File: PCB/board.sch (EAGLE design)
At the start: 9 parts, among them J1 PROG-HEADER_2X3_SHROUDED, J10 PROG-HEADER_2X5_1.27MM-SHROUD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, J2 PROG-HEADER_2X5_2.00MM-SHROUD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, J3 PROG-HEADER_2X5_SHROUDED, J5 PROG-HEADER_2X10_RIGHT-ANGLE, J6 PROG-HEADER_2X10_SHROUDED, J8 CONN-1X4, J9 CONN-1X6

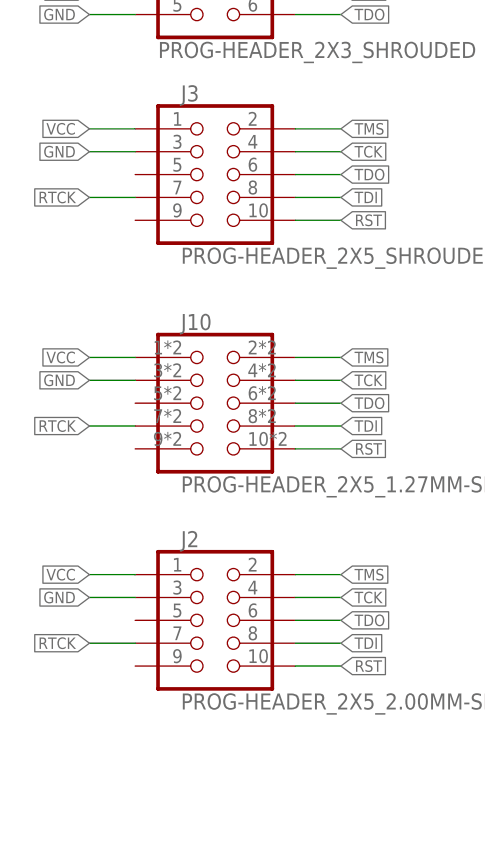
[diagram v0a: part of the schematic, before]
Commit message: connected pin 5, 9 to GND
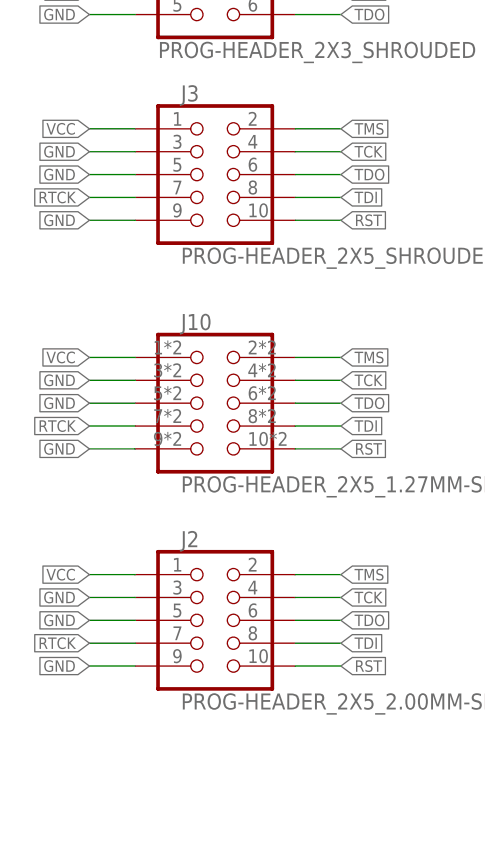
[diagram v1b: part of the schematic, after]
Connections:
- net GND: now also J10.5, J10.9, J2.5, J2.9, J3.5, J3.9
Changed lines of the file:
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@@
 <wire x1="207.01" y1="116.84" x2="201.93" y2="116.84" width="0.1524" layer="91"/>
+</segment>
+<segment>
+<wire x1="54.61" y1="123.19" x2="49.53" y2="123.19" width="0.1524" layer="91"/>
+<label x="49.53" y="123.19" size="1.27" layer="95" rot="R180" xref="yes"/>
+<pinref part="J3" gate="G$1" pin="5"/>
+</segment>
+<segment>
+<wire x1="54.61" y1="118.11" x2="49.53" y2="118.11" width="0.1524" layer="91"/>
+<label x="49.53" y="118.11" size="1.27" layer="95" rot="R180" xref="yes"/>
+<pinref part="J3" gate="G$1" pin="9"/>
+</segment>
+<segment>
+<wire x1="54.61" y1="97.79" x2="49.53" y2="97.79" width="0.1524" layer="91"/>
+<label x="49.53" y="97.79" size="1.27" layer="95" rot="R180" xref="yes"/>
+<pinref part="J10" gate="G$1" pin="5"/>
+</segment>
+<segment>
+<wire x1="54.61" y1="92.71" x2="49.53" y2="92.71" width="0.1524" layer="91"/>
+<label x="49.53" y="92.71" size="1.27" layer="95" rot="R180" xref="yes"/>
+<pinref part="J10" gate="G$1" pin="9"/>
+</segment>
+<segment>
+<wire x1="54.61" y1="73.66" x2="49.53" y2="73.66" width="0.1524" layer="91"/>
+<label x="49.53" y="73.66" size="1.27" layer="95" rot="R180" xref="yes"/>
+<pinref part="J2" gate="G$1" pin="5"/>
+</segment>
+<segment>
+<wire x1="54.61" y1="68.58" x2="49.53" y2="68.58" width="0.1524" layer="91"/>
+<label x="49.53" y="68.58" size="1.27" layer="95" rot="R180" xref="yes"/>
+<pinref part="J2" gate="G$1" pin="9"/>
 </segment>
 </net>

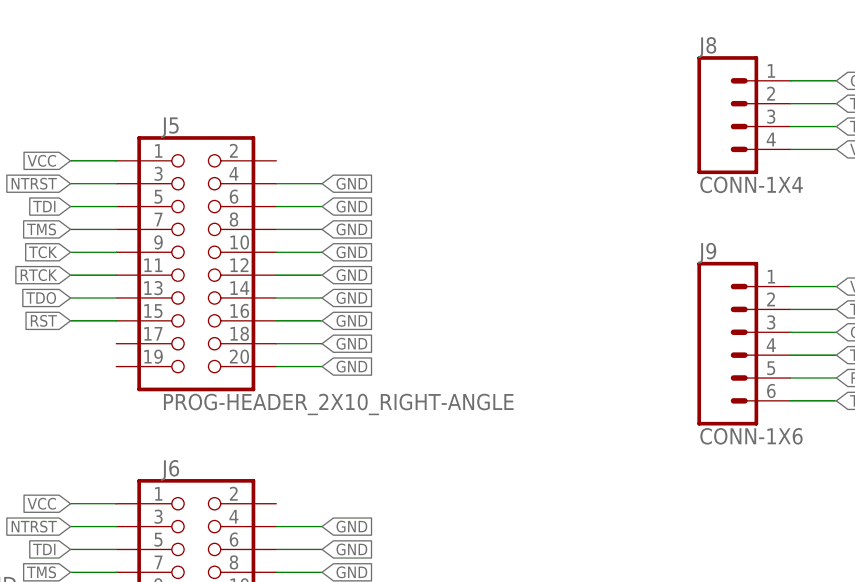
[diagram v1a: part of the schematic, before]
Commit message: changed right angle connector to end launch
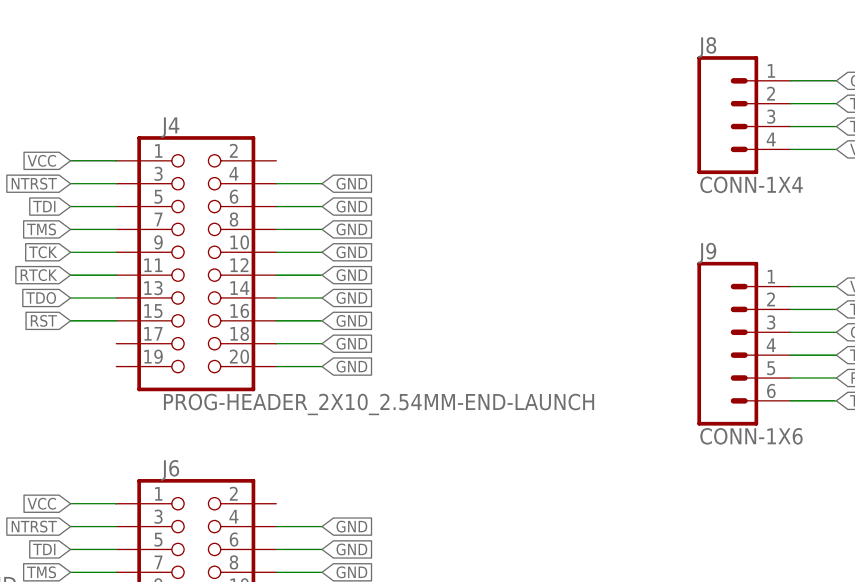
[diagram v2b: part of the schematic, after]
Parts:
- removed J5: PROG-HEADER_2X10_RIGHT-ANGLE, angrypig7-Connectors-Programming:PROG-HEADER_2X10_RIGHT-ANGLE
- added J4: PROG-HEADER_2X10_2.54MM-END-LAUNCH, angrypig7-Connectors-Programming:PROG-HEADER_2X10_2.54MM-END-LAUNCH
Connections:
- net GND: now also J4.10, J4.12, J4.14, J4.16, J4.18, J4.20, J4.4, J4.6, J4.8; no longer J5.10, J5.12, J5.14, J5.16, J5.18, J5.20, J5.4, J5.6, J5.8
- net NTRST: now also J4.3; no longer J5.3
- net RST: now also J4.15; no longer J5.15
- net RTCK: now also J4.11; no longer J5.11
- net TCK: now also J4.9; no longer J5.9
- net TDI: now also J4.5; no longer J5.5
- net TDO: now also J4.13; no longer J5.13
- net TMS: now also J4.7; no longer J5.7
- net VCC: now also J4.1; no longer J5.1
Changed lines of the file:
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@@
 <?xml version="1.0" encoding="utf-8"?>
 <!DOCTYPE eagle SYSTEM "eagle.dtd">
-<eagle version="9.6.0">
+<eagle version="9.6.1">
 <drawing>
 <settings>
@@
 <setting verticaltext="up"/>
 </settings>
-<grid distance="0.1" unitdist="inch" unit="inch" style="lines" multiple="1" display="no" altdistance="0.01" altunitdist="inch" altunit="inch"/>
+<grid distance="50" unitdist="mil" unit="mil" style="lines" multiple="1" display="no" altdistance="0.01" altunitdist="inch" altunit="inch"/>
 <layers>
 <layer number="1" name="Top" color="4" fill="1" visible="no" active="no"/>
@@
 <part name="J10" library="angrypig7-Connectors-Programming" deviceset="PROG-HEADER_2X5" device="_1.27MM-SHROUDED_PTH_SMD" value="PROG-HEADER_2X5_1.27MM-SHROUDED_PTH_SMD"/>
 <part name="J2" library="angrypig7-Connectors-Programming" deviceset="PROG-HEADER_2X5" device="_2.00MM-SHROUDED"/>
-<part name="J5" library="angrypig7-Connectors-Programming" deviceset="PROG-HEADER_2X10" device="_RIGHT-ANGLE"/>
+<part name="J4" library="angrypig7-Connectors-Programming" deviceset="PROG-HEADER_2X10" device="_2.54MM-END-LAUNCH"/>
 </parts>
 <sheets>
@@
 <attribute name="VALUE" x="59.69" y="63.754" size="1.778" layer="96" font="vector"/>
 </instance>
-<instance part="J5" gate="G$1" x="135.89" y="124.46" smashed="yes">
+<instance part="J4" gate="G$1" x="135.89" y="124.46" smashed="yes">
 <attribute name="NAME" x="132.08" y="138.938" size="1.778" layer="95" font="vector"/>
 <attribute name="VALUE" x="132.08" y="108.204" size="1.778" layer="96" font="vector"/>
@@
 <wire x1="127" y1="135.89" x2="121.92" y2="135.89" width="0.1524" layer="91"/>
 <label x="121.92" y="135.89" size="1.27" layer="95" rot="R180" xref="yes"/>
-<pinref part="J5" gate="G$1" pin="1"/>
+<pinref part="J4" gate="G$1" pin="1"/>
 </segment>
 </net>
@@
 <wire x1="127" y1="128.27" x2="121.92" y2="128.27" width="0.1524" layer="91"/>
 <label x="121.92" y="128.27" size="1.27" layer="95" rot="R180" xref="yes"/>
-<pinref part="J5" gate="G$1" pin="7"/>
+<pinref part="J4" gate="G$1" pin="7"/>
 </segment>
 <segment>
@@
 <wire x1="127" y1="120.65" x2="121.92" y2="120.65" width="0.1524" layer="91"/>
 <label x="121.92" y="120.65" size="1.27" layer="95" rot="R180" xref="yes"/>
-<pinref part="J5" gate="G$1" pin="13"/>
+<pinref part="J4" gate="G$1" pin="13"/>
 </segment>
 <segment>
@@
 <wire x1="127" y1="130.81" x2="121.92" y2="130.81" width="0.1524" layer="91"/>
 <label x="121.92" y="130.81" size="1.27" layer="95" rot="R180" xref="yes"/>
-<pinref part="J5" gate="G$1" pin="5"/>
+<pinref part="J4" gate="G$1" pin="5"/>
 </segment>
 </net>
@@
 <wire x1="127" y1="118.11" x2="121.92" y2="118.11" width="0.1524" layer="91"/>
 <label x="121.92" y="118.11" size="1.27" layer="95" rot="R180" xref="yes"/>
-<pinref part="J5" gate="G$1" pin="15"/>
+<pinref part="J4" gate="G$1" pin="15"/>
 </segment>
 <segment>
@@
 <wire x1="144.78" y1="133.35" x2="149.86" y2="133.35" width="0.1524" layer="91"/>
 <label x="149.86" y="133.35" size="1.27" layer="95" xref="yes"/>
-<pinref part="J5" gate="G$1" pin="4"/>
+<pinref part="J4" gate="G$1" pin="4"/>
 </segment>
 <segment>
 <wire x1="144.78" y1="130.81" x2="149.86" y2="130.81" width="0.1524" layer="91"/>
 <label x="149.86" y="130.81" size="1.27" layer="95" xref="yes"/>
-<pinref part="J5" gate="G$1" pin="6"/>
+<pinref part="J4" gate="G$1" pin="6"/>
 </segment>
 <segment>
 <wire x1="144.78" y1="113.03" x2="149.86" y2="113.03" width="0.1524" layer="91"/>
 <label x="149.86" y="113.03" size="1.27" layer="95" xref="yes"/>
-<pinref part="J5" gate="G$1" pin="20"/>
+<pinref part="J4" gate="G$1" pin="20"/>
 </segment>
 <segment>
 <wire x1="144.78" y1="115.57" x2="149.86" y2="115.57" width="0.1524" layer="91"/>
 <label x="149.86" y="115.57" size="1.27" layer="95" xref="yes"/>
-<pinref part="J5" gate="G$1" pin="18"/>
+<pinref part="J4" gate="G$1" pin="18"/>
 </segment>
 <segment>
 <wire x1="144.78" y1="118.11" x2="149.86" y2="118.11" width="0.1524" layer="91"/>
 <label x="149.86" y="118.11" size="1.27" layer="95" xref="yes"/>
-<pinref part="J5" gate="G$1" pin="16"/>
+<pinref part="J4" gate="G$1" pin="16"/>
 </segment>
 <segment>
 <wire x1="144.78" y1="120.65" x2="149.86" y2="120.65" width="0.1524" layer="91"/>
 <label x="149.86" y="120.65" size="1.27" layer="95" xref="yes"/>
-<pinref part="J5" gate="G$1" pin="14"/>
+<pinref part="J4" gate="G$1" pin="14"/>
 </segment>
 <segment>
 <wire x1="144.78" y1="123.19" x2="149.86" y2="123.19" width="0.1524" layer="91"/>
 <label x="149.86" y="123.19" size="1.27" layer="95" xref="yes"/>
-<pinref part="J5" gate="G$1" pin="12"/>
+<pinref part="J4" gate="G$1" pin="12"/>
 </segment>
 <segment>
 <wire x1="144.78" y1="125.73" x2="149.86" y2="125.73" width="0.1524" layer="91"/>
 <label x="149.86" y="125.73" size="1.27" layer="95" xref="yes"/>
-<pinref part="J5" gate="G$1" pin="10"/>
+<pinref part="J4" gate="G$1" pin="10"/>
 </segment>
 <segment>
 <wire x1="144.78" y1="128.27" x2="149.86" y2="128.27" width="0.1524" layer="91"/>
 <label x="149.86" y="128.27" size="1.27" layer="95" xref="yes"/>
-<pinref part="J5" gate="G$1" pin="8"/>
+<pinref part="J4" gate="G$1" pin="8"/>
 </segment>
 <segment>
@@
 <wire x1="127" y1="123.19" x2="121.92" y2="123.19" width="0.1524" layer="91"/>
 <label x="121.92" y="123.19" size="1.27" layer="95" rot="R180" xref="yes"/>
-<pinref part="J5" gate="G$1" pin="11"/>
+<pinref part="J4" gate="G$1" pin="11"/>
 </segment>
 </net>
@@
 <wire x1="127" y1="125.73" x2="121.92" y2="125.73" width="0.1524" layer="91"/>
 <label x="121.92" y="125.73" size="1.27" layer="95" rot="R180" xref="yes"/>
-<pinref part="J5" gate="G$1" pin="9"/>
+<pinref part="J4" gate="G$1" pin="9"/>
 </segment>
 <segment>
@@
 <net name="NTRST" class="0">
 <segment>
-<pinref part="J5" gate="G$1" pin="3"/>
 <wire x1="127" y1="133.35" x2="121.92" y2="133.35" width="0.1524" layer="91"/>
 <label x="121.92" y="133.35" size="1.27" layer="95" rot="R180" xref="yes"/>
-</segment>
-<segment>
+<pinref part="J4" gate="G$1" pin="3"/>
+</segment>
+<segment>

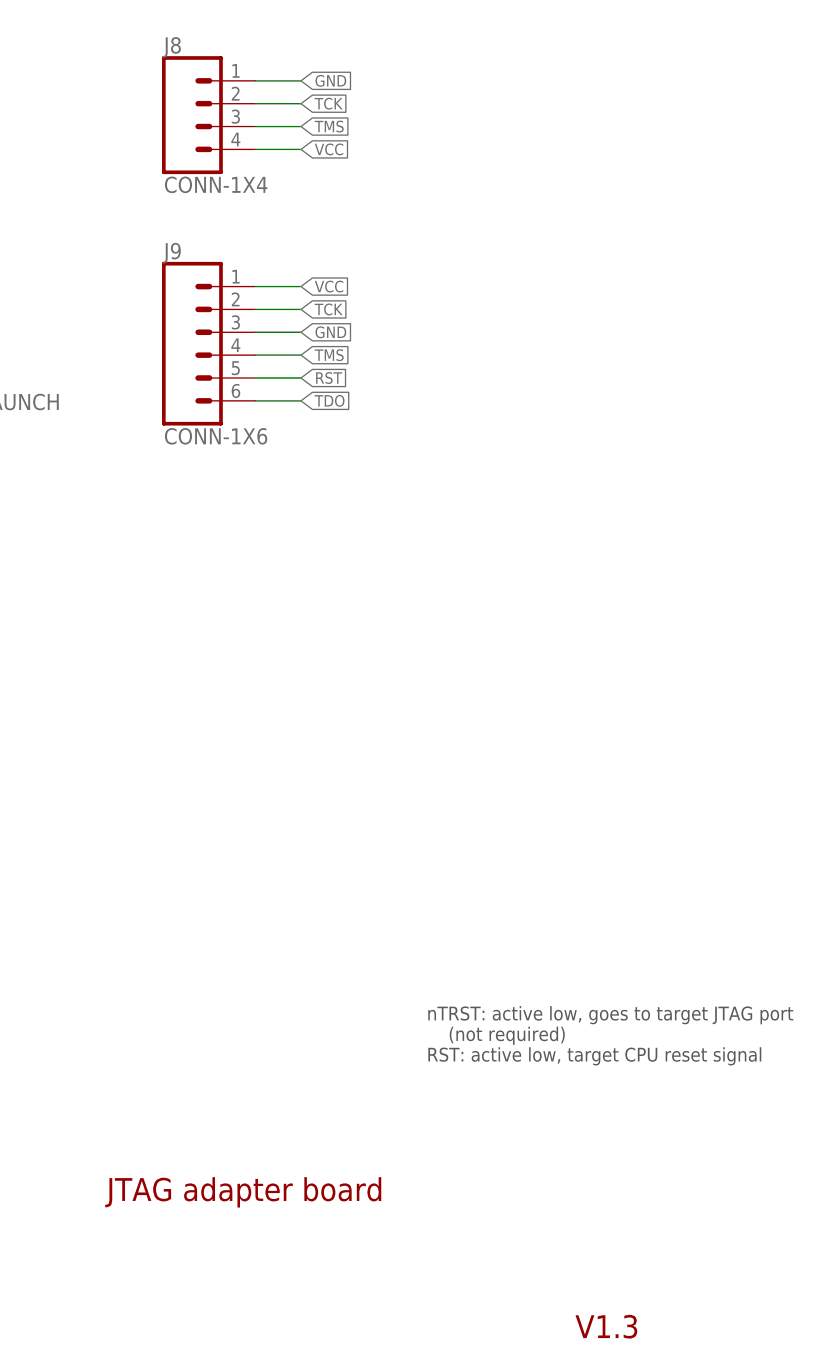
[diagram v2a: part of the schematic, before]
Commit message: fixed footprint error
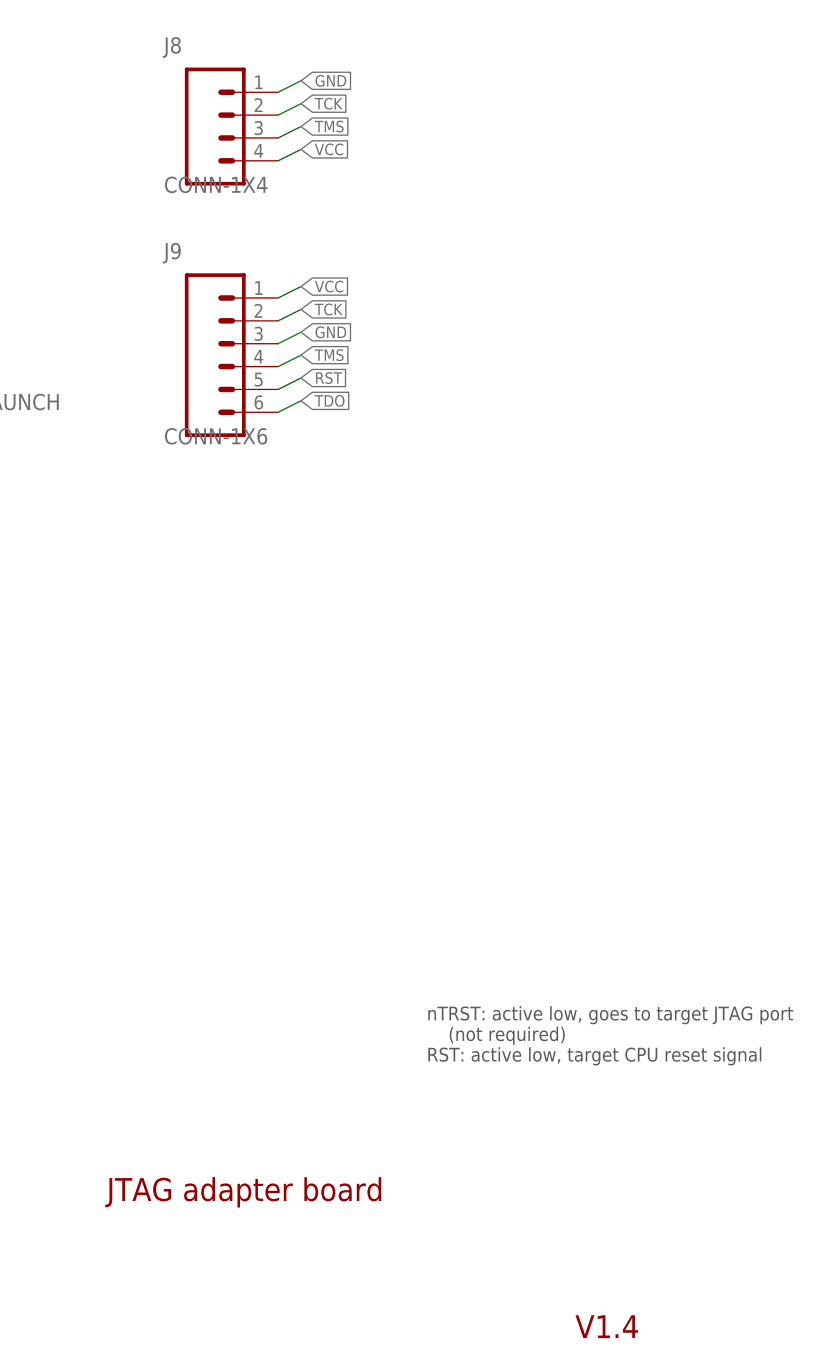
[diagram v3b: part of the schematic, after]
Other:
- moved on the sheet: J8, J9
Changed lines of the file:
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@@
 <attributes>
 <attribute name="CNAME" value="JTAG adapter board"/>
-<attribute name="CREVISION" value="V1.3"/>
+<attribute name="CREVISION" value="V1.4"/>
 </attributes>
 <variantdefs>
@@
 </segment>
 <segment>
-<wire x1="201.93" y1="137.16" x2="207.01" y2="137.16" width="0.1524" layer="91"/>
+<wire x1="204.47" y1="135.89" x2="207.01" y2="137.16" width="0.1524" layer="91"/>
 <label x="207.01" y="137.16" size="1.27" layer="95" xref="yes"/>
 <pinref part="J8" gate="G$1" pin="4"/>
@@
 <label x="207.01" y="121.92" size="1.27" layer="95" xref="yes"/>
 <pinref part="J9" gate="G$1" pin="1"/>
-<wire x1="207.01" y1="121.92" x2="201.93" y2="121.92" width="0.1524" layer="91"/>
+<wire x1="207.01" y1="121.92" x2="204.47" y2="120.65" width="0.1524" layer="91"/>
 </segment>
 <segment>
@@
 </segment>
 <segment>
-<wire x1="201.93" y1="139.7" x2="207.01" y2="139.7" width="0.1524" layer="91"/>
+<wire x1="204.47" y1="138.43" x2="207.01" y2="139.7" width="0.1524" layer="91"/>
 <label x="207.01" y="139.7" size="1.27" layer="95" xref="yes"/>
 <pinref part="J8" gate="G$1" pin="3"/>
@@
 <label x="207.01" y="114.3" size="1.27" layer="95" xref="yes"/>
 <pinref part="J9" gate="G$1" pin="4"/>
-<wire x1="201.93" y1="114.3" x2="207.01" y2="114.3" width="0.1524" layer="91"/>
+<wire x1="204.47" y1="113.03" x2="207.01" y2="114.3" width="0.1524" layer="91"/>
 </segment>
 </net>
@@
 <label x="207.01" y="109.22" size="1.27" layer="95" xref="yes"/>
 <pinref part="J9" gate="G$1" pin="6"/>
-<wire x1="201.93" y1="109.22" x2="207.01" y2="109.22" width="0.1524" layer="91"/>
+<wire x1="204.47" y1="107.95" x2="207.01" y2="109.22" width="0.1524" layer="91"/>
 </segment>
 </net>
@@
 <label x="207.01" y="111.76" size="1.27" layer="95" xref="yes"/>
 <pinref part="J9" gate="G$1" pin="5"/>
-<wire x1="201.93" y1="111.76" x2="207.01" y2="111.76" width="0.1524" layer="91"/>
+<wire x1="204.47" y1="110.49" x2="207.01" y2="111.76" width="0.1524" layer="91"/>
 </segment>
 </net>
@@
 </segment>
 <segment>
-<wire x1="201.93" y1="144.78" x2="207.01" y2="144.78" width="0.1524" layer="91"/>
+<wire x1="204.47" y1="143.51" x2="207.01" y2="144.78" width="0.1524" layer="91"/>
 <label x="207.01" y="144.78" size="1.27" layer="95" xref="yes"/>
 <pinref part="J8" gate="G$1" pin="1"/>
@@
 <label x="207.01" y="116.84" size="1.27" layer="95" xref="yes"/>
 <pinref part="J9" gate="G$1" pin="3"/>
-<wire x1="207.01" y1="116.84" x2="201.93" y2="116.84" width="0.1524" layer="91"/>
+<wire x1="207.01" y1="116.84" x2="204.47" y2="115.57" width="0.1524" layer="91"/>
 </segment>
 <segment>
@@
 <net name="TCK" class="0">
 <segment>
-<wire x1="201.93" y1="142.24" x2="207.01" y2="142.24" width="0.1524" layer="91"/>
+<wire x1="204.47" y1="140.97" x2="207.01" y2="142.24" width="0.1524" layer="91"/>
 <label x="207.01" y="142.24" size="1.27" layer="95" xref="yes"/>
 <pinref part="J8" gate="G$1" pin="2"/>
@@
 <label x="207.01" y="119.38" size="1.27" layer="95" xref="yes"/>
 <pinref part="J9" gate="G$1" pin="2"/>
-<wire x1="201.93" y1="119.38" x2="207.01" y2="119.38" width="0.1524" layer="91"/>
-</segment>
-</net>
+<wire x1="204.47" y1="118.11" x2="207.01" y2="119.38" width="0.1524" layer="91"/>
+</segment>
+</net>
